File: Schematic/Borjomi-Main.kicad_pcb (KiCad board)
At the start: 2 copper layers, 14 parts, among them J1 Vin 12V, J2 Gate 220V, J3 Vout 12V, J4 Data, J5 Pressure, U1 CAN_Module, U2 CurrentMeas_12V, U3 Relay_12Vout, U4 Relay_Gate220V, U5 Bluetooth

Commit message: Borjomi-main: almost final pcb
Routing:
- net Net-(A1-Pad19): track 0.00 -> 197.5 mm
- net Net-(A1-Pad27): track 90.1 -> 205.6 mm
- net Net-(A1-Pad21): track 0.00 -> 100.5 mm
- net Net-(A1-Pad6): track 0.00 -> 98.2 mm
- net Net-(A1-Pad10): track 0.00 -> 68.9 mm
- net Net-(J1-Pad2): track 0.00 -> 58.6 mm
- net Net-(A1-Pad13): track 0.00 -> 51.4 mm
- net Net-(J3-Pad2): track 0.00 -> 42.3 mm
- net Net-(A1-Pad7): track 0.00 -> 36.6 mm
- net Net-(U2-Pad5): track 0.00 -> 29.0 mm
- net Net-(D1-Pad1): track 0.00 -> 28.1 mm
- net GND: track 0.00 -> 11.5 mm
- net Net-(J4-Pad2): track 22.6 -> 23.7 mm
- added copper zone on B.Cu, net GND
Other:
- board outline added: 111.3 x 68.8 mm

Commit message: Borjomi-main PCB v1.0
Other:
- board text added: "+ 12V IN"
- board text added: "+ 12V OUT"
- board text added: "Borjomi Main v1.0"
- board text added: "Data"
- board text added: "Pressure"
- board text added: "Pump"
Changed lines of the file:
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@@
   (general
     (thickness 1.6)
-    (drawings 4)
+    (drawings 28)
     (tracks 153)
     (zones 0)
@@
     (34 B.Paste user hide)
     (35 F.Paste user hide)
-    (36 B.SilkS user)
+    (36 B.SilkS user hide)
     (37 F.SilkS user)
     (38 B.Mask user)
-    (39 F.Mask user)
+    (39 F.Mask user hide)
     (40 Dwgs.User user hide)
     (41 Cmts.User user hide)
@@
     (46 B.CrtYd user hide)
     (47 F.CrtYd user hide)
-    (48 B.Fab user)
-    (49 F.Fab user)
+    (48 B.Fab user hide)
+    (49 F.Fab user hide)
   )
   (setup
@@
     (descr "Arduino Nano, http://www.mouser.com/pdfdocs/Gravitech_Arduino_Nano3_0.pdf")
     (tags "Arduino Nano")
-    (fp_text reference A1 (at 7.62 -5.08) (layer F.SilkS)
+    (fp_text reference A1 (at 14.97584 41.05402) (layer F.SilkS)
       (effects (font (size 1 1) (thickness 0.15)))
     )
@@
     (descr "Diode, DO-27 series, Axial, Vertical, pin pitch=5.08mm, , length*diameter=9.52*5.33mm^2, , http://www.slottechforum.com/slotinfo/Techstuff/CD2%20Diodes%20and%20Transistors/Cases/Diode%20DO-27.jpg")
     (tags "Diode DO-27 series Axial Vertical pin pitch 5.08mm  length 9.52mm diameter 5.33mm")
-    (fp_text reference D1 (at 2.54 -3.785) (layer F.SilkS)
+    (fp_text reference D1 (at 8.4455 2.87274) (layer F.SilkS)
       (effects (font (size 1 1) (thickness 0.15)))
     )
@@
     (descr "Terminal Block Phoenix MKDS-1,5-2, 2 pins, pitch 5mm, size 10x9.8mm^2, drill diamater 1.3mm, pad diameter 2.6mm, see http://www.farnell.com/datasheets/100425.pdf, script-generated using https://github.com/pointhi/kicad-footprint-generator/scripts/TerminalBlock_Phoenix")
     (tags "THT Terminal Block Phoenix MKDS-1,5-2 pitch 5mm size 10x9.8mm^2 drill 1.3mm pad 2.6mm")
-    (fp_text reference J1 (at 2.5 -6.26) (layer F.SilkS)
+    (fp_text reference J1 (at 7.18312 -5.25272) (layer F.SilkS)
       (effects (font (size 1 1) (thickness 0.15)))
     )
@@
     (descr "Terminal Block Phoenix MKDS-1,5-2, 2 pins, pitch 5mm, size 10x9.8mm^2, drill diamater 1.3mm, pad diameter 2.6mm, see http://www.farnell.com/datasheets/100425.pdf, script-generated using https://github.com/pointhi/kicad-footprint-generator/scripts/TerminalBlock_Phoenix")
     (tags "THT Terminal Block Phoenix MKDS-1,5-2 pitch 5mm size 10x9.8mm^2 drill 1.3mm pad 2.6mm")
-    (fp_text reference J2 (at 2.5 -6.26) (layer F.SilkS)
+    (fp_text reference J2 (at 7.15772 -5.32892) (layer F.SilkS)
       (effects (font (size 1 1) (thickness 0.15)))
     )
@@
     (descr "Terminal Block Phoenix MKDS-1,5-2, 2 pins, pitch 5mm, size 10x9.8mm^2, drill diamater 1.3mm, pad diameter 2.6mm, see http://www.farnell.com/datasheets/100425.pdf, script-generated using https://github.com/pointhi/kicad-footprint-generator/scripts/TerminalBlock_Phoenix")
     (tags "THT Terminal Block Phoenix MKDS-1,5-2 pitch 5mm size 10x9.8mm^2 drill 1.3mm pad 2.6mm")
-    (fp_text reference J3 (at 2.5 -6.26) (layer F.SilkS)
+    (fp_text reference J3 (at 7.24916 -5.34416) (layer F.SilkS)
       (effects (font (size 1 1) (thickness 0.15)))
     )
@@
     (descr "RJ12 connector  https://cdn.amphenol-icc.com/media/wysiwyg/files/drawing/c-bmj-0082.pdf")
     (tags "RJ12 connector")
-    (fp_text reference J4 (at -1.67 -2.16) (layer F.SilkS)
+    (fp_text reference J4 (at 9.3472 -2.31902) (layer F.SilkS)
       (effects (font (size 1 1) (thickness 0.15)))
     )
@@
     (descr "RJ12 connector  https://cdn.amphenol-icc.com/media/wysiwyg/files/drawing/c-bmj-0082.pdf")
     (tags "RJ12 connector")
-    (fp_text reference J5 (at -1.67 -2.16) (layer F.SilkS)
+    (fp_text reference J5 (at 9.46912 -2.15392) (layer F.SilkS)
       (effects (font (size 1 1) (thickness 0.15)))
     )
@@
   (module CAN:AOC346_MCP2515_Holes0.9 (layer F.Cu)
     (at 209.55 138.176 90)
-    (fp_text reference U1 (at 20.32 -15.24 90) (layer F.SilkS)
+    (fp_text reference U1 (at -3.10642 1.89484 180) (layer F.SilkS)
       (effects (font (size 1 1) (thickness 0.15)))
     )
@@
   (module ACS_CurrentSensor:ACS712 (layer F.Cu)
     (at 162.687 137.287 90)
-    (fp_text reference U2 (at 13.97 8.89 90) (layer F.SilkS)
+    (fp_text reference U2 (at -4.00304 0.0127 180) (layer F.SilkS)
       (effects (font (size 1 1) (thickness 0.15)))
     )
@@
   (module RelayModule:Relay_Module_1_Channel_Holes0.9 (layer F.Cu)
     (at 142.24 118.872 90)
-    (fp_text reference U3 (at -0.127 -9.271 90) (layer F.SilkS)
+    (fp_text reference U3 (at -22.41804 -0.01524 180) (layer F.SilkS)
       (effects (font (size 1 1) (thickness 0.15)))
     )
@@
   (module RelayModule:Relay_Module_1_Channel_Holes0.9 (layer F.Cu)
     (at 121.666 118.872 90)
-    (fp_text reference U4 (at 0 -10.16 90) (layer F.SilkS)
+    (fp_text reference U4 (at -22.40534 -0.1905 180) (layer F.SilkS)
       (effects (font (size 1 1) (thickness 0.15)))
     )
@@
     (pad 6 thru_hole circle (at 0 6.35 180) (size 1.8 1.8) (drill 0.9) (layers *.Cu *.Mask))
   )
+  (gr_text "Borjomi\nMain\nv1.0" (at 162.82162 100.7745) (layer F.SilkS)
+    (effects (font (size 2 2) (thickness 0.3)))
+  )
+  (gr_text Data (at 221.15272 94.42958) (layer F.SilkS)
+    (effects (font (size 1 1) (thickness 0.15)))
+  )
+  (gr_text Pressure (at 203.2 94.39402) (layer F.SilkS)
+    (effects (font (size 1 1) (thickness 0.15)))
+  )
+  (gr_text "+ 12V IN" (at 143.4973 83.24088) (layer F.SilkS)
+    (effects (font (size 1 1) (thickness 0.15)))
+  )
+  (gr_text "+ 12V OUT" (at 132.207 83.40344) (layer F.SilkS)
+    (effects (font (size 1 1) (thickness 0.15)))
+  )
+  (gr_text Pump (at 121.88444 83.4009) (layer F.SilkS)
+    (effects (font (size 1 1) (thickness 0.15)))
+  )
+  (gr_line (start 140.415 78.105) (end 135.422 83.098) (layer B.Mask) (width 2))
+  (gr_line (start 135.422 83.098) (end 135.422 95.417) (layer B.Mask) (width 2))
+  (gr_line (start 135.422 95.417) (end 137.922 97.917) (layer B.Mask) (width 2))
+  (gr_line (start 137.922 97.917) (end 147.955 97.917) (layer B.Mask) (width 2))
+  (gr_line (start 147.955 97.917) (end 160.147 110.109) (layer B.Mask) (width 2))
+  (gr_line (start 160.147 110.109) (end 160.147 113.287) (layer B.Mask) (width 2))
+  (gr_line (start 165.227 113.287) (end 165.227 114.842634) (layer B.Mask) (width 2))
+  (gr_line (start 165.227 114.842634) (end 162.975634 117.094) (layer B.Mask) (width 2))
+  (gr_line (start 162.975634 117.094) (end 154.813 117.094) (layer B.Mask) (width 2))
+  (gr_line (start 154.813 117.094) (end 147.32 109.601) (layer B.Mask) (width 2))
+  (gr_line (start 147.32 109.601) (end 147.32 104.072) (layer B.Mask) (width 2))
+  (gr_line (start 128.731 97.997) (end 128.731 78.105) (layer B.Mask) (width 2))
+  (gr_line (start 131.953 101.219) (end 128.731 97.997) (layer B.Mask) (width 2))
+  (gr_line (start 139.387 101.219) (end 131.953 101.219) (layer B.Mask) (width 2))
+  (gr_line (start 142.24 104.072) (end 139.387 101.219) (layer B.Mask) (width 2))
+  (gr_line (start 143.0782 75.7682) (end 145.415 78.105) (layer B.Mask) (width 1))
+  (gr_line (start 133.731 78.105) (end 136.0678 75.7682) (layer B.Mask) (width 1))
+  (gr_line (start 136.0678 75.7682) (end 143.0782 75.7682) (layer B.Mask) (width 1))
   (gr_line (start 112.649 143.637) (end 112.649 74.803) (layer Edge.Cuts) (width 0.1))
   (gr_line (start 223.901 143.637) (end 112.649 143.637) (layer Edge.Cuts) (width 0.1))

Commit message: Fix few bugs
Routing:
- net GND: track 11.5 -> 26.0 mm
- net Net-(A1-Pad27): track 205.6 -> 203.8 mm
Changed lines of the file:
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@@
     (thickness 1.6)
     (drawings 28)
-    (tracks 153)
+    (tracks 155)
     (zones 0)
     (modules 14)
@@
   )
   (setup
-    (last_trace_width 0.25)
+    (last_trace_width 0.6)
     (user_trace_width 0.2)
     (user_trace_width 0.3)
@@
     (visible_elements FFFFFF7F)
     (pcbplotparams
-      (layerselection 0x010fc_ffffffff)
-      (usegerberextensions false)
+      (layerselection 0x01060_fffffffe)
+      (usegerberextensions true)
       (usegerberattributes false)
       (usegerberadvancedattributes false)
       (creategerberjobfile false)
       (excludeedgelayer true)
-      (linewidth 0.100000)
+      (linewidth 0.150000)
       (plotframeref false)
       (viasonmask false)
@@
       (psa4output false)
       (plotreference true)
-      (plotvalue true)
+      (plotvalue false)
       (plotinvisibletext false)
       (padsonsilk false)
@@
       (outputformat 1)
       (mirror false)
-      (drillshape 1)
+      (drillshape 0)
       (scaleselection 1)
-      (outputdirectory ""))
+      (outputdirectory "gerber/main-v1.0/"))
   )
   (net 0 "")
@@
   (gr_line (start 112.649 74.803) (end 223.901 74.803) (layer Edge.Cuts) (width 0.1))
   (segment (start 187.198 125.984) (end 188.976 125.984) (width 0.3) (layer B.Cu) (net 1))
+  (segment (start 183.388 97.028) (end 183.388 122.174) (width 0.3) (layer B.Cu) (net 1))
   (segment (start 183.388 122.174) (end 187.198 125.984) (width 0.3) (layer B.Cu) (net 1))
-  (segment (start 183.388 97.028) (end 183.388 122.174) (width 0.3) (layer B.Cu) (net 1))
-  (segment (start 179.324 91.567) (end 187.178001 83.712999) (width 0.3) (layer B.Cu) (net 1))
-  (segment (start 122.936 138.43) (end 122.936 134.366) (width 0.3) (layer B.Cu) (net 1))
+  (segment (start 190.119 90.297) (end 183.388 97.028) (width 0.3) (layer B.Cu) (net 1))
   (segment (start 125.095 139.192) (end 123.698 139.192) (width 0.3) (layer B.Cu) (net 1))
   (segment (start 132.207 132.08) (end 125.095 139.192) (width 0.3) (layer B.Cu) (net 1))
+  (segment (start 187.178001 83.712999) (end 189.718001 83.712999) (width 0.3) (layer B.Cu) (net 1))
+  (segment (start 159.385 132.08) (end 132.207 132.08) (width 0.3) (layer B.Cu) (net 1))
+  (segment (start 123.698 139.192) (end 122.93092 138.42492) (width 0.3) (layer B.Cu) (net 1))
+  (segment (start 162.687 135.382) (end 159.385 132.08) (width 0.3) (layer B.Cu) (net 1))
+  (segment (start 122.93092 138.42492) (end 122.93092 134.37108) (width 0.3) (layer B.Cu) (net 1))
+  (segment (start 177.292 112.014) (end 179.324 109.982) (width 0.3) (layer B.Cu) (net 1))
   (segment (start 190.119 84.113998) (end 190.119 90.297) (width 0.3) (layer B.Cu) (net 1))
+  (segment (start 128.778 128.524) (end 156.464 128.524) (width 0.3) (layer B.Cu) (net 1))
+  (segment (start 172.974 112.014) (end 177.292 112.014) (width 0.3) (layer B.Cu) (net 1))
+  (segment (start 179.324 109.982) (end 179.324 91.567) (width 0.3) (layer B.Cu) (net 1))
+  (segment (start 179.324 91.567) (end 187.178001 83.712999) (width 0.3) (layer B.Cu) (net 1))
   (segment (start 162.687 137.287) (end 162.687 135.382) (width 0.3) (layer B.Cu) (net 1))
-  (segment (start 190.119 90.297) (end 183.388 97.028) (width 0.3) (layer B.Cu) (net 1))
+  (segment (start 122.93092 134.37108) (end 128.778 128.524) (width 0.3) (layer B.Cu) (net 1))
+  (segment (start 156.464 128.524) (end 172.974 112.014) (width 0.3) (layer B.Cu) (net 1))
   (segment (start 189.718001 83.712999) (end 190.119 84.113998) (width 0.3) (layer B.Cu) (net 1))
-  (segment (start 159.385 132.08) (end 132.207 132.08) (width 0.3) (layer B.Cu) (net 1))
-  (segment (start 162.687 135.382) (end 159.385 132.08) (width 0.3) (layer B.Cu) (net 1))
-  (segment (start 122.936 134.366) (end 128.778 128.524) (width 0.3) (layer B.Cu) (net 1))
-  (segment (start 128.778 128.524) (end 156.464 128.524) (width 0.3) (layer B.Cu) (net 1))
-  (segment (start 156.464 128.524) (end 172.974 112.014) (width 0.3) (layer B.Cu) (net 1))
-  (segment (start 172.974 112.014) (end 177.292 112.014) (width 0.3) (layer B.Cu) (net 1))
-  (segment (start 177.292 112.014) (end 179.324 109.982) (width 0.3) (layer B.Cu) (net 1))
-  (segment (start 123.698 139.192) (end 122.936 138.43) (width 0.3) (layer B.Cu) (net 1))
-  (segment (start 187.178001 83.712999) (end 189.718001 83.712999) (width 0.3) (layer B.Cu) (net 1))
-  (segment (start 179.324 109.982) (end 179.324 91.567) (width 0.3) (layer B.Cu) (net 1))
+  (segment (start 133.731 78.105) (end 136.0678 75.7682) (width 1) (layer B.Cu) (net 2))
+  (segment (start 143.0782 75.7682) (end 145.415 78.105) (width 1) (layer B.Cu) (net 2))
   (segment (start 161.417 136.525) (end 161.417 138.049) (width 0.25) (layer B.Cu) (net 2))
   (segment (start 188.341 82.55) (end 188.468 82.423) (width 0.6) (layer B.Cu) (net 2))
@@
   (segment (start 143.3905 138.4225) (end 142.24 137.272) (width 0.6) (layer B.Cu) (net 2))
   (segment (start 142.24 137.272) (end 141.041 136.073) (width 0.6) (layer B.Cu) (net 2))
+  (segment (start 133.731 78.105) (end 131.73202 78.105) (width 1) (layer B.Cu) (net 2))
+  (segment (start 133.731 78.105) (end 133.731 79.87284) (width 1) (layer B.Cu) (net 2))
+  (segment (start 145.415 78.105) (end 145.415 80.15224) (width 1) (layer B.Cu) (net 2))
+  (segment (start 145.415 78.105) (end 147.47494 78.105) (width 1) (layer B.Cu) (net 2))
   (segment (start 142.24 93.98) (end 145.415 90.805) (width 0.3) (layer B.Cu) (net 3))
   (segment (start 140.462 93.98) (end 142.24 93.98) (width 0.3) (layer B.Cu) (net 3))
@@
   (segment (start 171.831 110.744) (end 173.736 110.744) (width 0.3) (layer B.Cu) (net 4))
   (segment (start 156.718 125.857) (end 171.831 110.744) (width 0.3) (layer B.Cu) (net 4))
-  (segment (start 120.326001 133.673999) (end 128.143 125.857) (width 0.3) (layer B.Cu) (net 4))
+  (segment (start 128.143 125.857) (end 156.718 125.857) (width 0.3) (layer B.Cu) (net 4))
+  (segment (start 120.39854 133.60146) (end 128.143 125.857) (width 0.3) (layer B.Cu) (net 4))
+  (segment (start 144.78 137.272) (end 141.112 133.604) (width 0.3) (layer B.Cu) (net 4))
+  (segment (start 141.112 133.604) (end 133.477 133.604) (width 0.3) (layer B.Cu) (net 4))
+  (segment (start 126.238 140.843) (end 121.793 140.843) (width 0.3) (layer B.Cu) (net 4))
   (segment (start 133.477 133.604) (end 126.238 140.843) (width 0.3) (layer B.Cu) (net 4))
-  (segment (start 128.143 125.857) (end 156.718 125.857) (width 0.3) (layer B.Cu) (net 4))
-  (segment (start 141.112 133.604) (end 133.477 133.604) (width 0.3) (layer B.Cu) (net 4))
-  (segment (start 144.78 137.272) (end 141.112 133.604) (width 0.3) (layer B.Cu) (net 4))
-  (segment (start 126.238 140.843) (end 121.793 140.843) (width 0.3) (layer B.Cu) (net 4))
-  (segment (start 121.793 140.843) (end 120.326001 139.376001) (width 0.3) (layer B.Cu) (net 4))
-  (segment (start 120.326001 139.376001) (end 120.326001 133.673999) (width 0.3) (layer B.Cu) (net 4))
+  (segment (start 121.793 140.843) (end 120.39854 139.44854) (width 0.3) (layer B.Cu) (net 4))
+  (segment (start 120.39854 139.44854) (end 120.39854 133.60146) (width 0.3) (layer B.Cu) (net 4))
   (segment (start 180.721 92.71) (end 188.468 84.963) (width 0.3) (layer B.Cu) (net 5))
   (segment (start 180.721 109.982) (end 180.721 92.71) (width 0.3) (layer B.Cu) (net 5))
@@
   (segment (start 190.248792 105.664) (end 200.406 95.506792) (width 0.6) (layer B.Cu) (net 9))
   (segment (start 188.976 105.664) (end 190.248792 105.664) (width 0.6) (layer B.Cu) (net 9))
-  (segment (start 134.732 142.24) (end 139.7 137.272) (width 0.6) (layer B.Cu) (net 9))
-  (segment (start 121.285 142.24) (end 134.732 142.24) (width 0.6) (layer B.Cu) (net 9))
-  (segment (start 119.126 137.272) (end 119.126 140.081) (width 0.6) (layer B.Cu) (net 9))
-  (segment (start 119.126 140.081) (end 121.285 142.24) (width 0.6) (layer B.Cu) (net 9))
-  (segment (start 160.147 139.573) (end 160.147 137.287) (width 0.6) (layer B.Cu) (net 9))
-  (segment (start 162.687 142.113) (end 160.147 139.573) (width 0.6) (layer B.Cu) (net 9))
-  (segment (start 215.265 142.113) (end 162.687 142.113) (width 0.6) (layer B.Cu) (net 9))
+  (segment (start 119.126 137.272) (end 119.126 139.2301) (width 0.6) (layer B.Cu) (net 9))
+  (segment (start 119.126 139.2301) (end 122.0089 142.113) (width 0.6) (layer B.Cu) (net 9))
   (segment (start 217.17 138.176) (end 217.17 140.208) (width 0.6) (layer B.Cu) (net 9))
   (segment (start 217.17 140.208) (end 215.265 142.113) (width 0.6) (layer B.Cu) (net 9))
-  (segment (start 144.795 142.367) (end 139.7 137.272) (width 0.6) (layer B.Cu) (net 9))
-  (segment (start 157.226 142.367) (end 144.795 142.367) (width 0.6) (layer B.Cu) (net 9))
-  (segment (start 160.147 137.287) (end 160.147 139.446) (width 0.6) (layer B.Cu) (net 9))
-  (segment (start 160.147 139.446) (end 157.226 142.367) (width 0.6) (layer B.Cu) (net 9))
+  (segment (start 139.7 137.272) (end 139.7 142.113) (width 0.6) (layer B.Cu) (net 9))
+  (segment (start 160.147 142.00632) (end 160.25368 142.113) (width 0.6) (layer B.Cu) (net 9))
+  (segment (start 160.147 137.287) (end 160.147 142.00632) (width 0.6) (layer B.Cu) (net 9))
+  (segment (start 215.265 142.113) (end 160.25368 142.113) (width 0.6) (layer B.Cu) (net 9))
+  (segment (start 160.25368 142.113) (end 122.0089 142.113) (width 0.6) (layer B.Cu) (net 9))
   (segment (start 211.190001 137.276001) (end 212.09 138.176) (width 0.3) (layer B.Cu) (net 10))
   (segment (start 203.708 129.794) (end 211.190001 137.276001) (width 0.3) (layer B.Cu) (net 10))

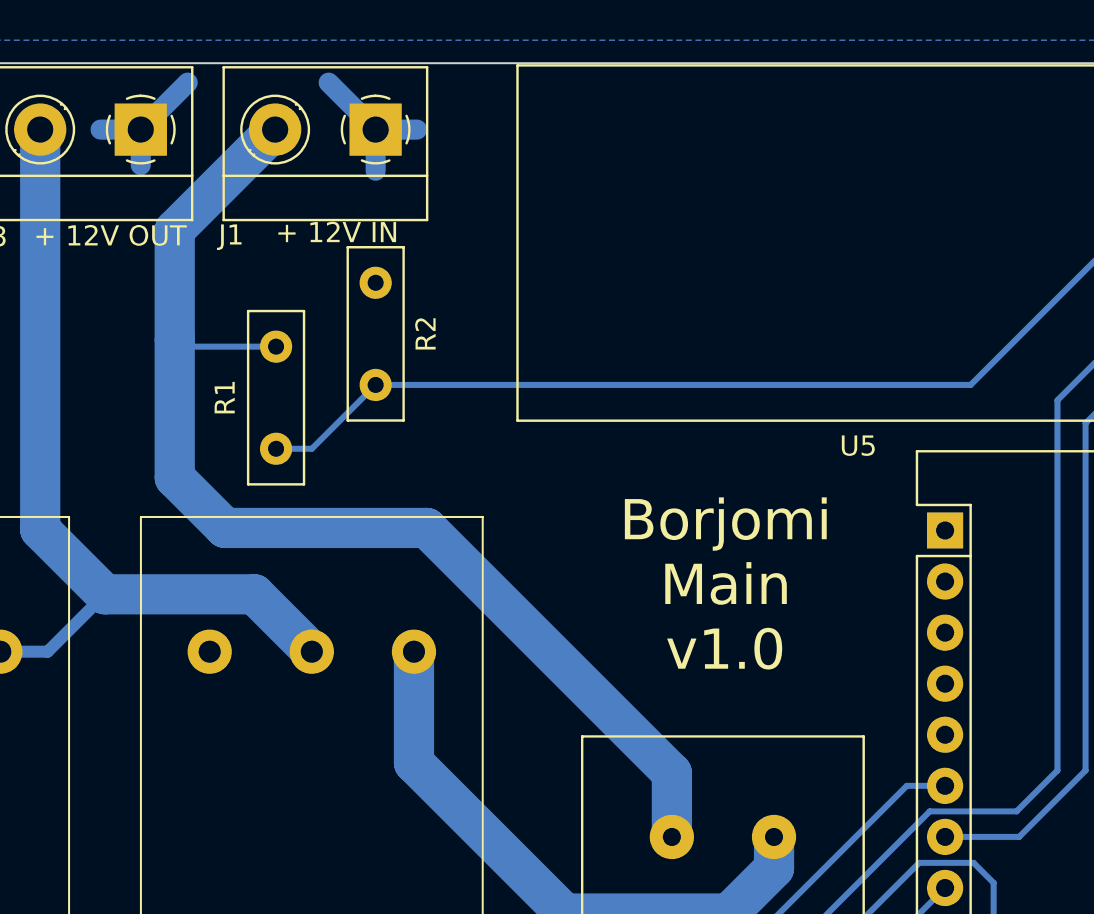
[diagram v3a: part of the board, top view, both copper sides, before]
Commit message: Update schematics/pcb to use barrel_connector as 12V IN
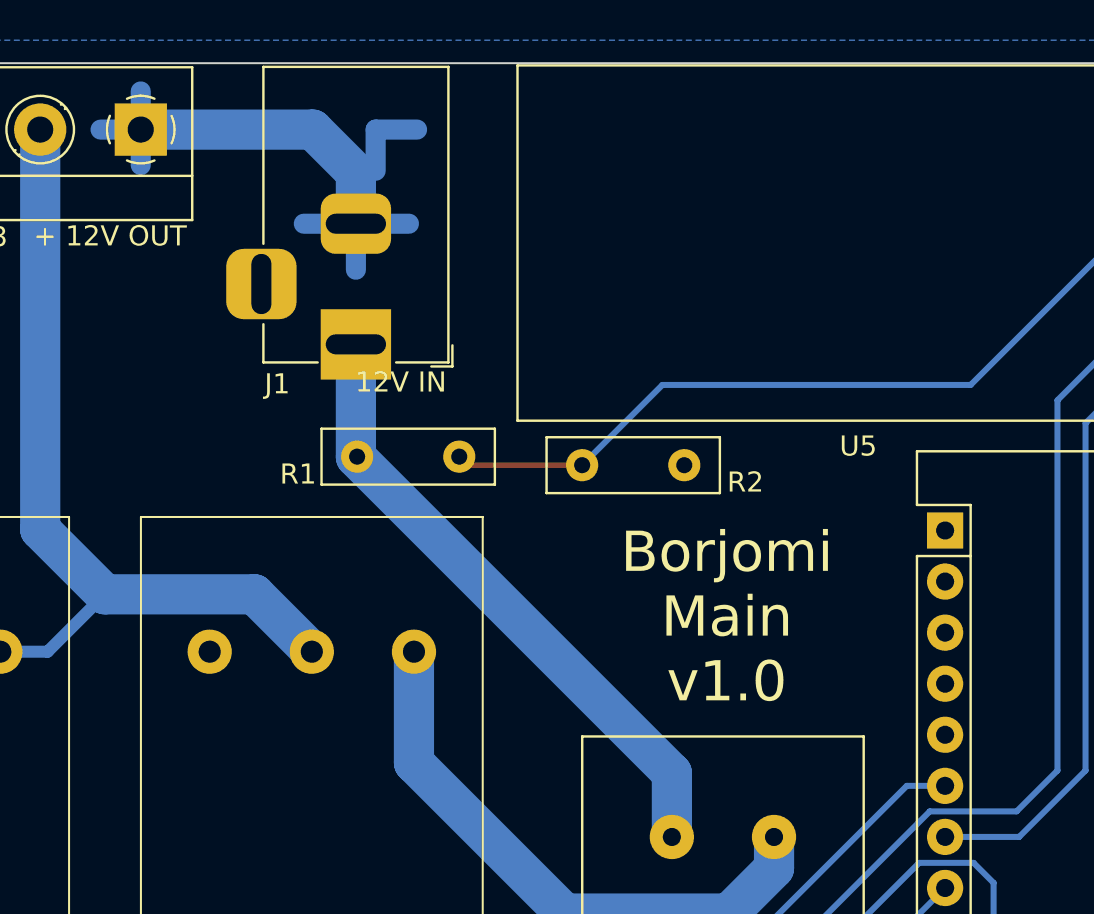
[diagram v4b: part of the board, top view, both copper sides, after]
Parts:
- J1: footprint Connector:Degson_DG301_1x02_P5.00mm_Horizontal -> Connector_BarrelJack:BarrelJack_Horizontal
- moved R2 17.8 mm to (160.8, 94.8), turned to 180 degrees
- moved J1 10.7 mm to (144.4, 88.8), turned to 270 degrees
- moved R1 9.12 mm to (149.6, 94.4), turned to 180 degrees
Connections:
- J1 pad 1: GND -> Net-(J1-Pad1)
- J1 pad 2: Net-(J1-Pad2) -> GND
- R1 pad 2: Net-(J1-Pad2) -> Net-(J1-Pad1)
- U2 pad 4: Net-(J1-Pad2) -> Net-(J1-Pad1)
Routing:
- net Net-(J1-Pad2): track 58.6 -> 0.00 mm
- net Net-(J1-Pad1): track 0.00 -> 31.0 mm
- net GND: track 26.0 -> 42.9 mm
- net Net-(A1-Pad21): track 100.5 -> 91.9 mm
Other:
- board text added: "12V IN"
- board text removed: "+ 12V IN"
